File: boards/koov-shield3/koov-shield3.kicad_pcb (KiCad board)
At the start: 2 copper layers, 68.6 x 53.3 mm, 28 parts, among them J1 Power, J2 Digital/PWM, J3 Analog, J4 Digital/PWM, SW1 SW_DPDT

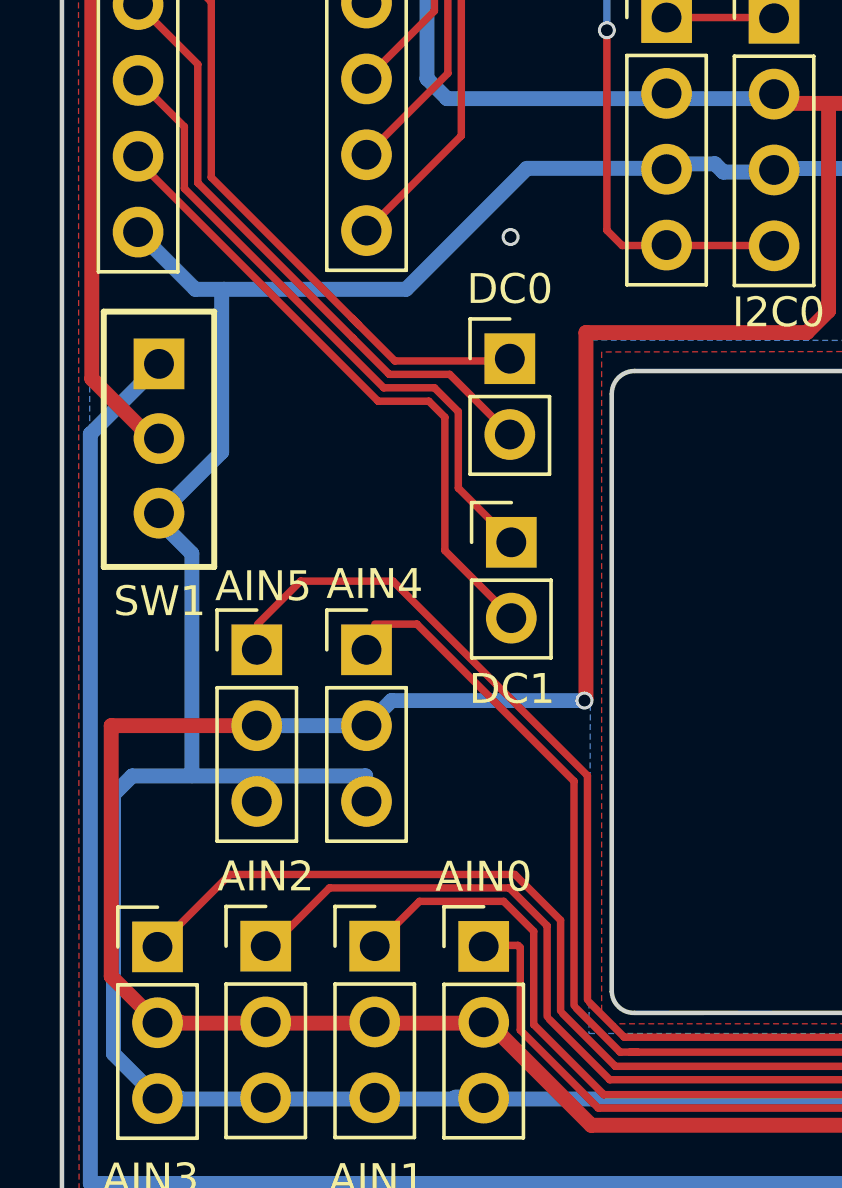
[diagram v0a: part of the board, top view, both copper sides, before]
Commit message: Correct DC motor connector position.
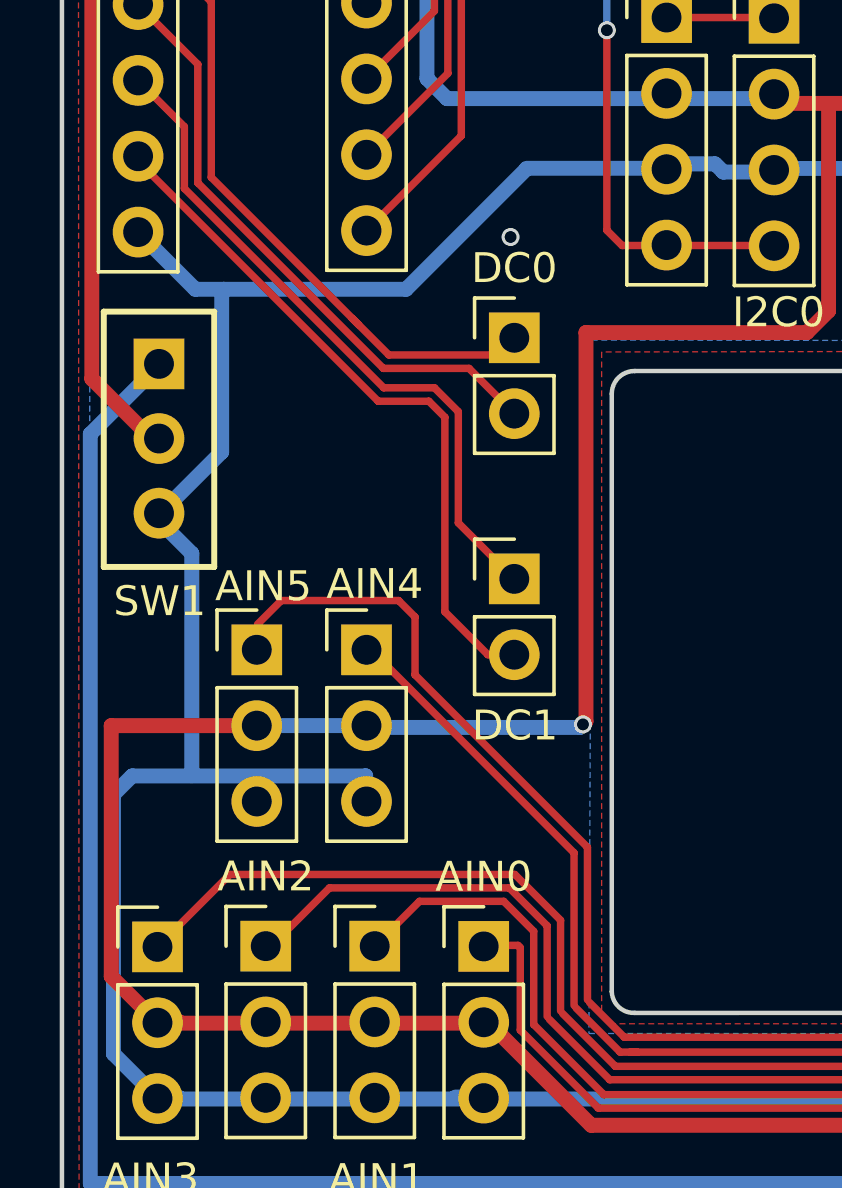
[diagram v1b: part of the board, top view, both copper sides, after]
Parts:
- moved DC1 1.23 mm to (115.2, 74.9)
- moved DC0 0.72 mm to (115.2, 66.8)
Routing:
- net /DC1_OUT1: track 21.5 -> 23.4 mm
- net /DC1_OUT0: track 21.5 -> 22.9 mm
- net /A4: track 63.7 -> 62.4 mm
- net /A5: track 71.1 -> 70.3 mm
- net /DC0_OUT0: track 22.0 -> 22.5 mm
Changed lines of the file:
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@@
 	(footprint "Connector_PinHeader_2.54mm:PinHeader_1x02_P2.54mm_Vertical"
 		(layer "F.Cu")
-		(at 115.05 73.7)
+		(at 115.15 74.925)
 		(descr "Through hole straight pin header, 1x02, 2.54mm pitch, single row")
 		(tags "Through hole pin header THT 1x02 2.54mm single row")
@@
 	(footprint "Connector_PinHeader_2.54mm:PinHeader_1x02_P2.54mm_Vertical"
 		(layer "F.Cu")
-		(at 115 67.55)
+		(at 115.15 66.85)
 		(descr "Through hole straight pin header, 1x02, 2.54mm pitch, single row")
 		(tags "Through hole pin header THT 1x02 2.54mm single row")
@@
 	)
 	(segment
-		(start 117.5 79)
-		(end 117.55 78.95)
+		(start 117.725432 93.225)
+		(end 114.275432 89.775)
 		(width 0.5)
 		(layer "F.Cu")
@@
 	)
 	(segment
-		(start 117.725432 93.225)
-		(end 114.275432 89.775)
+		(start 114.125 89.775)
+		(end 114.095 89.805)
 		(width 0.5)
 		(layer "F.Cu")
@@
 	)
 	(segment
-		(start 117.55 66.675)
-		(end 124.95 66.675)
+		(start 125.675 65.95)
+		(end 125.675 59.165)
 		(width 0.5)
 		(layer "F.Cu")
@@
 	)
 	(segment
-		(start 114.125 89.775)
-		(end 114.095 89.805)
+		(start 117.45 79.8)
+		(end 117.55 79.7)
 		(width 0.5)
 		(layer "F.Cu")
@@
 	)
 	(segment
+		(start 124.95 66.675)
+		(end 125.675 65.95)
+		(width 0.5)
+		(layer "F.Cu")
+		(net 9)
+	)
+	(segment
 		(start 103.215 89.805)
 		(end 103.2 89.79)
@@
 	)
 	(segment
-		(start 117.55 78.95)
+		(start 117.55 79.7)
 		(end 117.55 66.675)
 		(width 0.5)
@@
 	)
 	(segment
-		(start 125.675 65.95)
-		(end 125.675 59.165)
-		(width 0.5)
-		(layer "F.Cu")
-		(net 9)
-	)
-	(segment
-		(start 124.95 66.675)
-		(end 125.675 65.95)
+		(start 117.55 66.675)
+		(end 124.95 66.675)
 		(width 0.5)
 		(layer "F.Cu")
@@
 	)
 	(via
-		(at 117.5 79)
+		(at 117.45 79.8)
 		(size 0.6)
 		(drill 0.4)
@@
 	)
 	(segment
+		(start 110.26 79.9)
+		(end 110.2 79.84)
+		(width 0.5)
+		(layer "B.Cu")
+		(net 9)
+	)
+	(segment
 		(start 112.225 52.585)
 		(end 112.225 58.168478)
@@
 	)
 	(segment
-		(start 112.896522 58.84)
-		(end 123.7 58.84)
+		(start 117.35 79.9)
+		(end 110.26 79.9)
 		(width 0.5)
 		(layer "B.Cu")
@@
 	)
 	(segment
-		(start 111.04 79)
-		(end 110.2 79.84)
+		(start 117.45 79.8)
+		(end 117.35 79.9)
 		(width 0.5)
 		(layer "B.Cu")
@@
 	)
 	(segment
-		(start 117.5 79)
-		(end 111.04 79)
+		(start 112.896522 58.84)
+		(end 123.7 58.84)
 		(width 0.5)
 		(layer "B.Cu")
@@
 	)
 	(segment
-		(start 111.888604 76.44)
-		(end 117.15 81.701396)
+		(start 110.478604 76.953604)
+		(end 110.478604 77.428604)
 		(width 0.25)
 		(layer "F.Cu")
@@
 	)
 	(segment
-		(start 110.478604 76.44)
-		(end 111.888604 76.44)
-		(width 0.25)
-		(layer "F.Cu")
-		(net 10)
-	)
-	(segment
-		(start 117.15 81.701396)
+		(start 117.15 84.1)
 		(end 117.15 89.206802)
 		(width 0.25)
@@
 	)
 	(segment
+		(start 110.478604 77.428604)
+		(end 117.15 84.1)
+		(width 0.25)
+		(layer "F.Cu")
+		(net 10)
+	)
+	(segment
 		(start 157.05 93.55)
 		(end 160.96 97.46)
@@
 	)
 	(segment
-		(start 117.6 81.515)
-		(end 111.085 75)
+		(start 111.825 76.2)
+		(end 111.275 75.65)
 		(width 0.25)
 		(layer "F.Cu")
@@
 	)
 	(segment
-		(start 111.085 75)
-		(end 107.995 75)
+		(start 117.6 89.020406)
+		(end 117.6 83.913604)
 		(width 0.25)
 		(layer "F.Cu")
@@
 	)
 	(segment
+		(start 117.6 83.913604)
+		(end 111.825 78.138604)
+		(width 0.25)
+		(layer "F.Cu")
+		(net 22)
+	)
+	(segment
 		(start 118.83198 90.275)
 		(end 132.370152 90.275)
@@
 	)
 	(segment
-		(start 117.673896 89.116916)
-		(end 118.83198 90.275)
+		(start 111.275 75.65)
+		(end 107.345 75.65)
 		(width 0.25)
 		(layer "F.Cu")
@@
 	)
 	(segment
-		(start 117.6 89.020406)
-		(end 117.6 81.515)
+		(start 117.673896 89.116916)
+		(end 118.83198 90.275)
 		(width 0.25)
 		(layer "F.Cu")
@@
 	)
 	(segment
-		(start 107.995 75)
+		(start 111.825 78.138604)
+		(end 111.825 76.2)
+		(width 0.25)
+		(layer "F.Cu")
+		(net 22)
+	)
+	(segment
+		(start 107.345 75.65)
 		(end 106.55 76.445)
 		(width 0.25)
@@
 	)
 	(segment
-		(start 105 61.475812)
-		(end 109.934188 66.41)
+		(start 110.949188 67.425)
+		(end 114.575 67.425)
 		(width 0.25)
 		(layer "F.Cu")
@@
 	)
 	(segment
-		(start 111.149188 67.625)
-		(end 114.775 67.625)
+		(start 105 61.475812)
+		(end 109.934188 66.41)
 		(width 0.25)
 		(layer "F.Cu")
@@
 	(segment
 		(start 109.724594 66.200406)
-		(end 111.149188 67.625)
+		(end 110.949188 67.425)
 		(width 0.25)
 		(layer "F.Cu")
@@
 	)
 	(segment
-		(start 104.55 57.69)
-		(end 104.55 61.662208)
+		(start 114.575 67.425)
+		(end 115.15 66.85)
 		(width 0.25)
 		(layer "F.Cu")
-		(net 27)
+		(net 24)
 	)
 	(segment
-		(start 109.747792 66.86)
-		(end 110.962792 68.075)
+		(start 102.55 55.69)
+		(end 104.55 57.69)
 		(width 0.25)
 		(layer "F.Cu")
@@
 	)
 	(segment
-		(start 102.55 55.69)
-		(end 104.55 57.69)
+		(start 110.762792 67.875)
+		(end 113.635 67.875)
 		(width 0.25)
 		(layer "F.Cu")
@@
 	)
 	(segment
-		(start 112.985 68.075)
-		(end 115 70.09)
+		(start 104.55 57.69)
+		(end 104.55 61.662208)
 		(width 0.25)
 		(layer "F.Cu")
@@
 	)
 	(segment
-		(start 110.962792 68.075)
-		(end 112.985 68.075)
+		(start 104.55 61.662208)
+		(end 110.762792 67.875)
 		(width 0.25)
 		(layer "F.Cu")
@@
 	)
 	(segment
-		(start 104.55 61.662208)
-		(end 109.747792 66.86)
+		(start 113.635 67.875)
+		(end 115 69.24)
 		(width 0.25)
 		(layer "F.Cu")
@@
 	)
 	(segment
-		(start 110.776396 68.525)
-		(end 112.475 68.525)
+		(start 113.275 73.05)
+		(end 115.15 74.925)
 		(width 0.25)
 		(layer "F.Cu")
@@
 	)
 	(segment
-		(start 113.275 69.325)
-		(end 113.275 71.885)
+		(start 102.55 58.23)
+		(end 104.1 59.78)
 		(width 0.25)
 		(layer "F.Cu")
@@
 	)
 	(segment
-		(start 113.275 71.885)
-		(end 114.975 73.585)
+		(start 112.475 68.525)
+		(end 113.275 69.325)
+		(width 0.25)
+		(layer "F.Cu")
+		(net 28)
+	)
+	(segment
+		(start 104.1 61.848604)
+		(end 110.776396 68.525)
 		(width 0.25)
 		(layer "F.Cu")
@@
 	)
 	(segment
-		(start 104.1 61.848604)
-		(end 110.776396 68.525)
+		(start 110.776396 68.525)
+		(end 112.475 68.525)
 		(width 0.25)
 		(layer "F.Cu")
@@
 	)
 	(segment
-		(start 112.475 68.525)
-		(end 113.275 69.325)
+		(start 113.275 69.325)
+		(end 113.275 73.05)
 		(width 0.25)
 		(layer "F.Cu")
@@
 	)
 	(segment
-		(start 102.55 58.23)
-		(end 104.1 59.78)
+		(start 110.59 68.975)
+		(end 112.288604 68.975)
 		(width 0.25)
 		(layer "F.Cu")
-		(net 28)
+		(net 29)
 	)
 	(segment
-		(start 112.288604 68.975)
-		(end 112.825 69.511396)
+		(start 112.825 76.025)
+		(end 114.265 77.465)
 		(width 0.25)
 		(layer "F.Cu")
@@
 	)
 	(segment
-		(start 112.825 69.511396)
-		(end 112.825 73.975)
+		(start 114.265 77.465)
+		(end 115.15 77.465)
 		(width 0.25)
 		(layer "F.Cu")
@@
 	)
 	(segment
-		(start 102.55 60.77)
-		(end 102.55 60.935)
+		(start 102.55 60.935)
+		(end 110.59 68.975)
 		(width 0.25)
 		(layer "F.Cu")
@@
 	)
 	(segment
-		(start 110.59 68.975)
-		(end 112.288604 68.975)
+		(start 112.288604 68.975)
+		(end 112.825 69.511396)
 		(width 0.25)
 		(layer "F.Cu")
@@
 	)
 	(segment
-		(start 102.55 60.935)
-		(end 110.59 68.975)
+		(start 112.825 69.511396)
+		(end 112.825 76.025)
 		(width 0.25)
 		(layer "F.Cu")
@@
 	)
 	(segment
-		(start 112.825 73.975)
-		(end 114.975 76.125)
+		(start 102.55 60.77)
+		(end 102.55 60.935)
 		(width 0.25)
 		(layer "F.Cu")

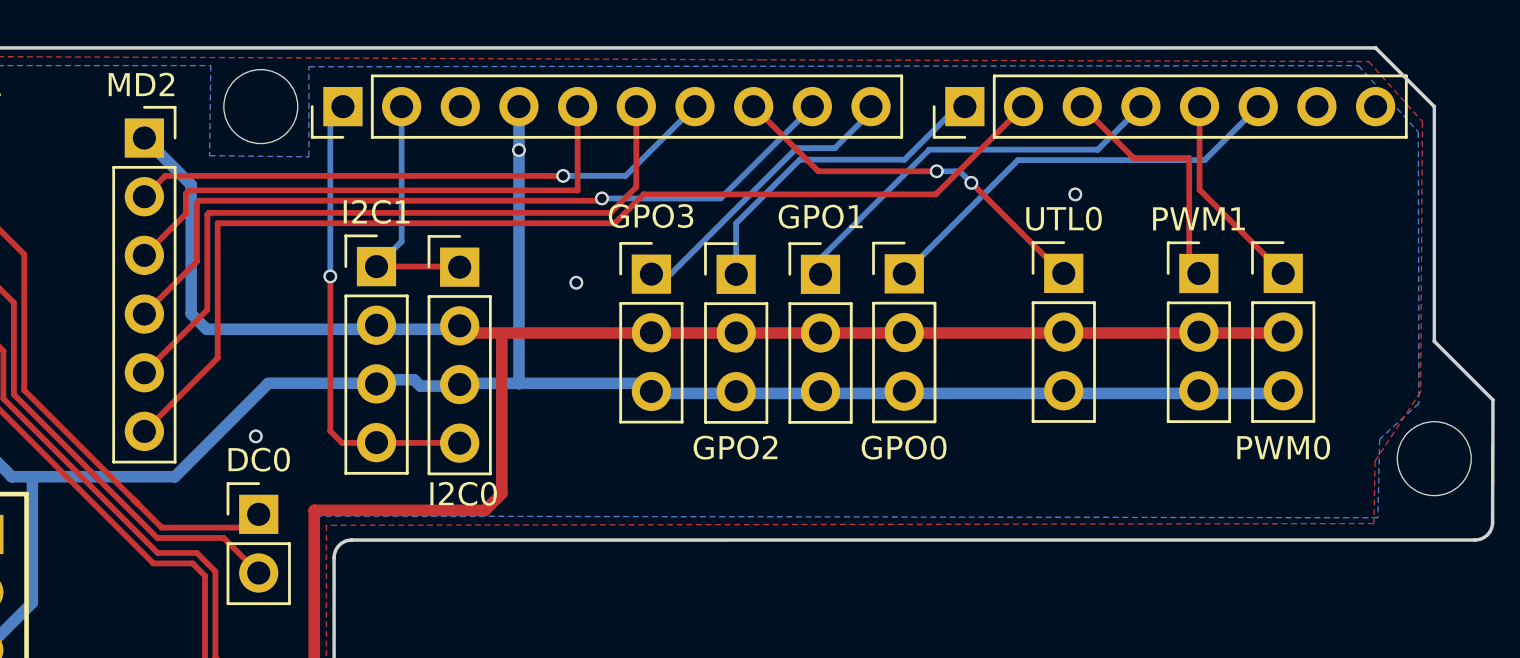
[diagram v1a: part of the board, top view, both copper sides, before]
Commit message: Support reverse-insertion-proof.
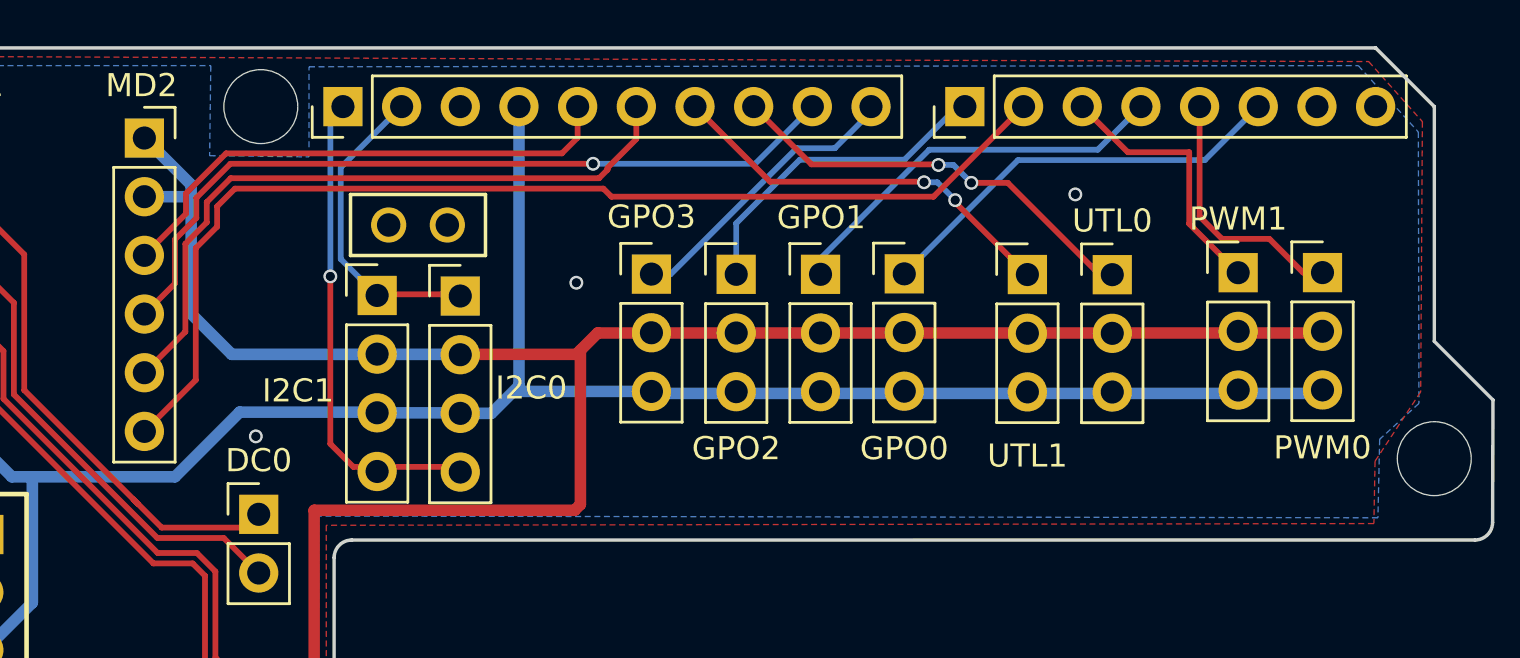
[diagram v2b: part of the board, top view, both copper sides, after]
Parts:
- added REF**: CONN_RS1-02-G_ADM, Connector:CONN_RS1-02-G_ADM, F.Cu at (120.8, 54.3)
- added UTL1: Conn_01x03, Connector_PinHeader_2.54mm:PinHeader_1x03_P2.54mm_Vertical, F.Cu at (148.4, 56.5)
- moved UTL0 2.10 mm to (152.1, 56.5)
- moved PWM1 1.70 mm to (157.6, 56.4)
- moved PWM0 1.70 mm to (161.2, 56.4)
- moved I2C0 1.25 mm to (123.9, 57.4)
- moved I2C1 1.25 mm to (120.3, 57.4)
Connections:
- MD2 pad 2: /11 -> +3.3V
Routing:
- net +3.3V: track 146.5 -> 154.3 mm
- net /11: track 25.5 -> 17.7 mm, vias 1 -> 2
- net /SDA: track 10.3 -> 13.2 mm
- net /*3: track 8.72 -> 11.1 mm
- net /*10: track 16.4 -> 18.5 mm
- net /13: track 24.1 -> 22.7 mm
- net GND: track 159.1 -> 159.9 mm, vias 4 -> 3
- net /12: track 30.5 -> 29.7 mm
- net /SCL: track 19.4 -> 20.2 mm
- net /*6: track 47.3 -> 48.0 mm
- net /*5: track 10.9 -> 11.5 mm

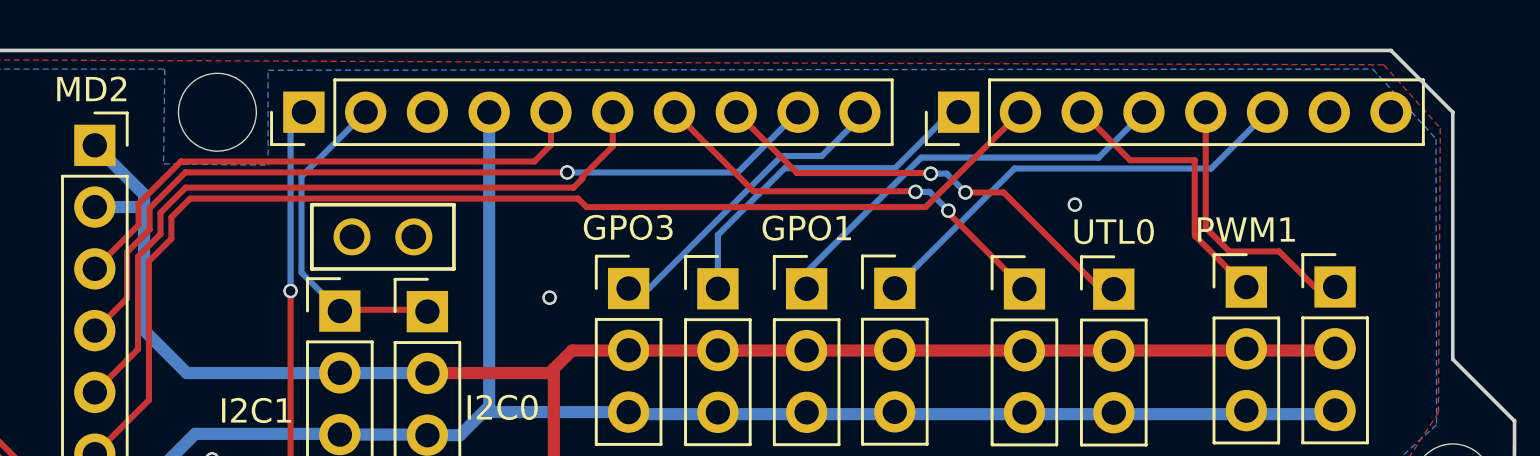
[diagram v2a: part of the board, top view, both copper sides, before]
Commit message: Wiring UARTs to the unused connector.
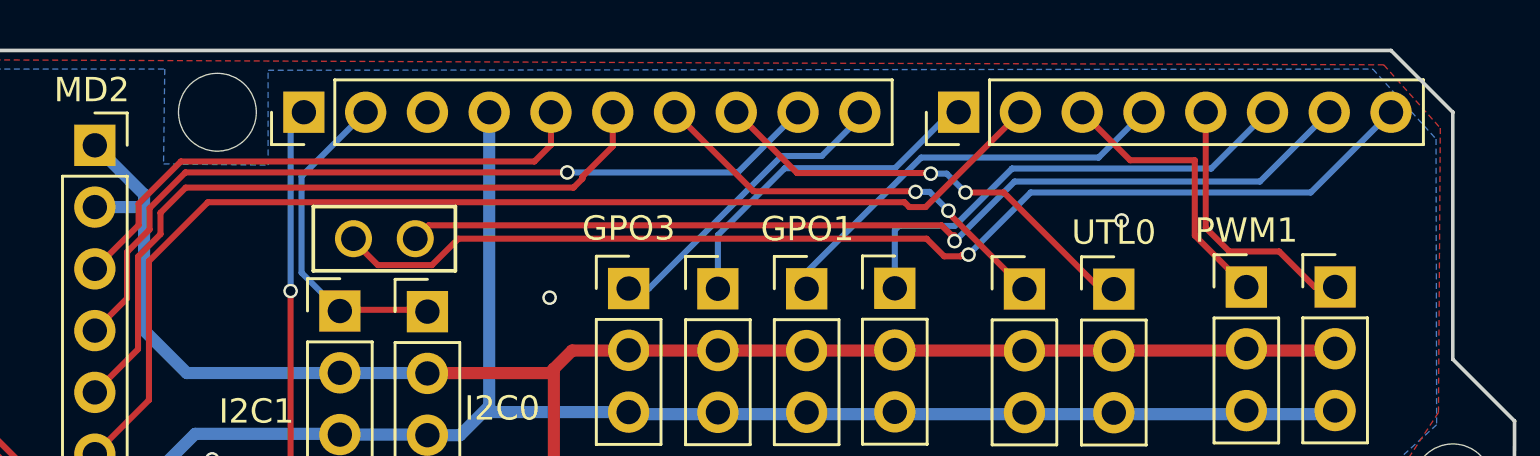
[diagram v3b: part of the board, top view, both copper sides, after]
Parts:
- removed REF**: CONN_RS1-02-G_ADM, Connector:CONN_RS1-02-G_ADM
- added J5: RS1-02-G, Connector:CONN_RS1-02-G_ADM, F.Cu at (120.8, 54.4)
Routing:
- net /0: track 0.00 -> 46.4 mm, vias 0 -> 1
- net /1: track 0.00 -> 40.6 mm, vias 0 -> 1
- net /2: track 18.3 -> 19.7 mm
- net /*6: track 48.0 -> 47.4 mm
